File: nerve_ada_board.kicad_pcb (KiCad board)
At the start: 4 copper layers, 100 x 100 mm, 66 parts, among them J1 TC2050-IDC, J10 PC1-3, J11 PB4-5, J12 Camera, J2 472192001, J3 2171750001, J6 WS2812B, J7 CAN1, J8 CAN2, J9 PA4-7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

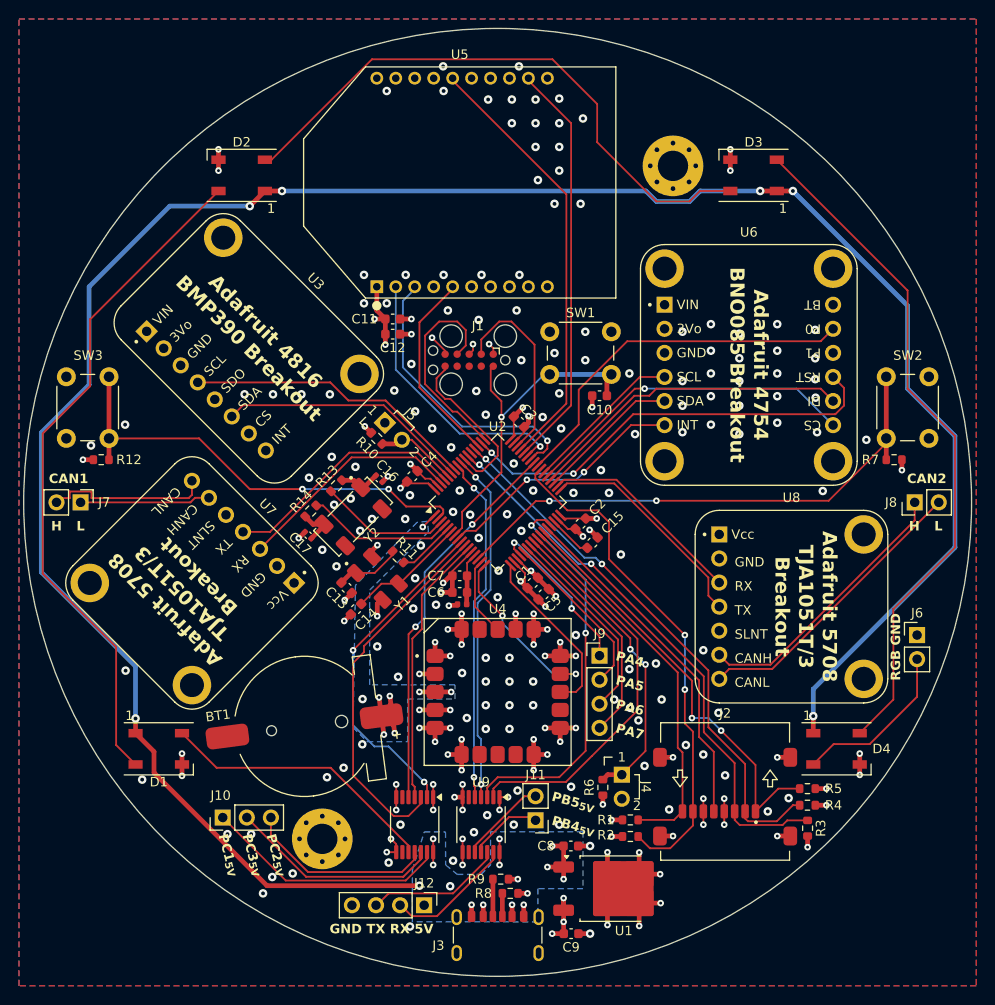
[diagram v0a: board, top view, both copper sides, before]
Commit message: Add GND plane stitching and cleanup layout
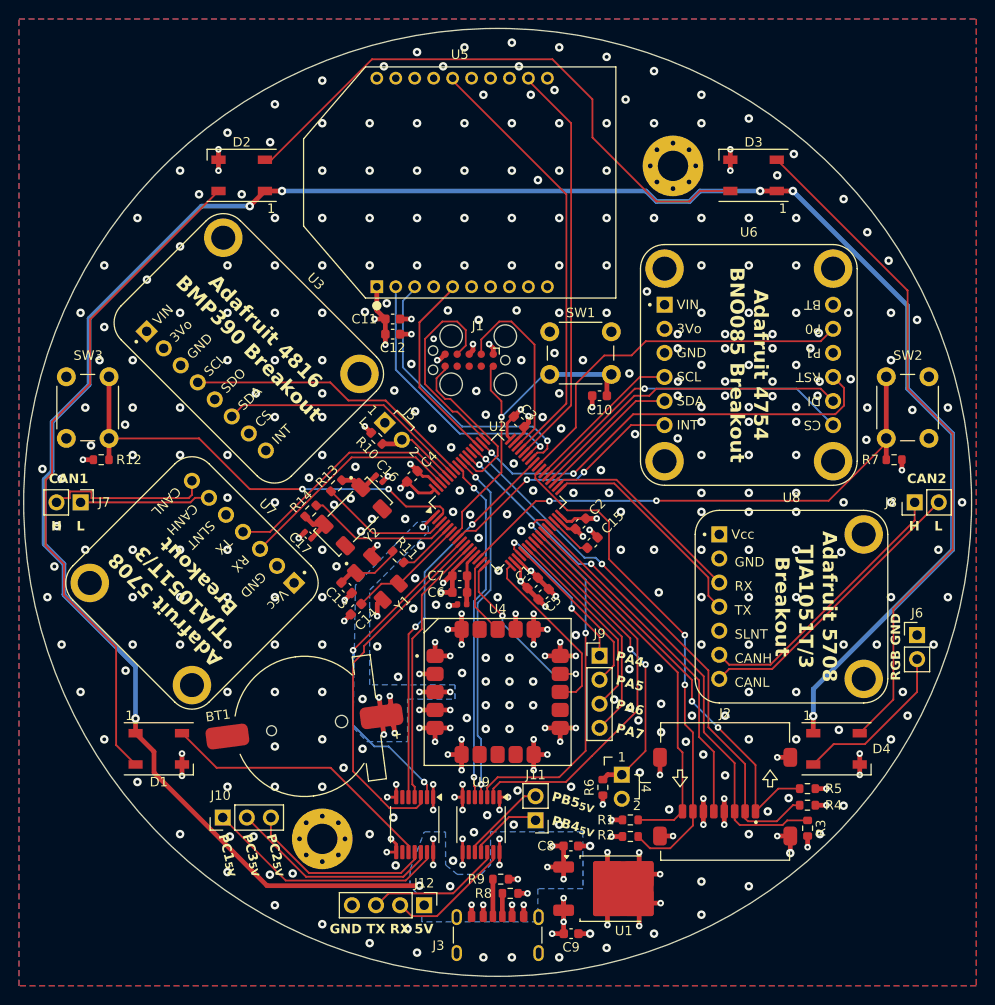
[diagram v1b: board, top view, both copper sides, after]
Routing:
- net +5V: track 255.4 -> 253.0 mm
- net /SDIO_D2: track 45.4 -> 44.4 mm
- net /PC2: track 39.3 -> 38.4 mm
- net /GPIO_IMU_P0: track 39.4 -> 39.9 mm
- net GND: track 126.7 -> 126.3 mm, vias 233 -> 402

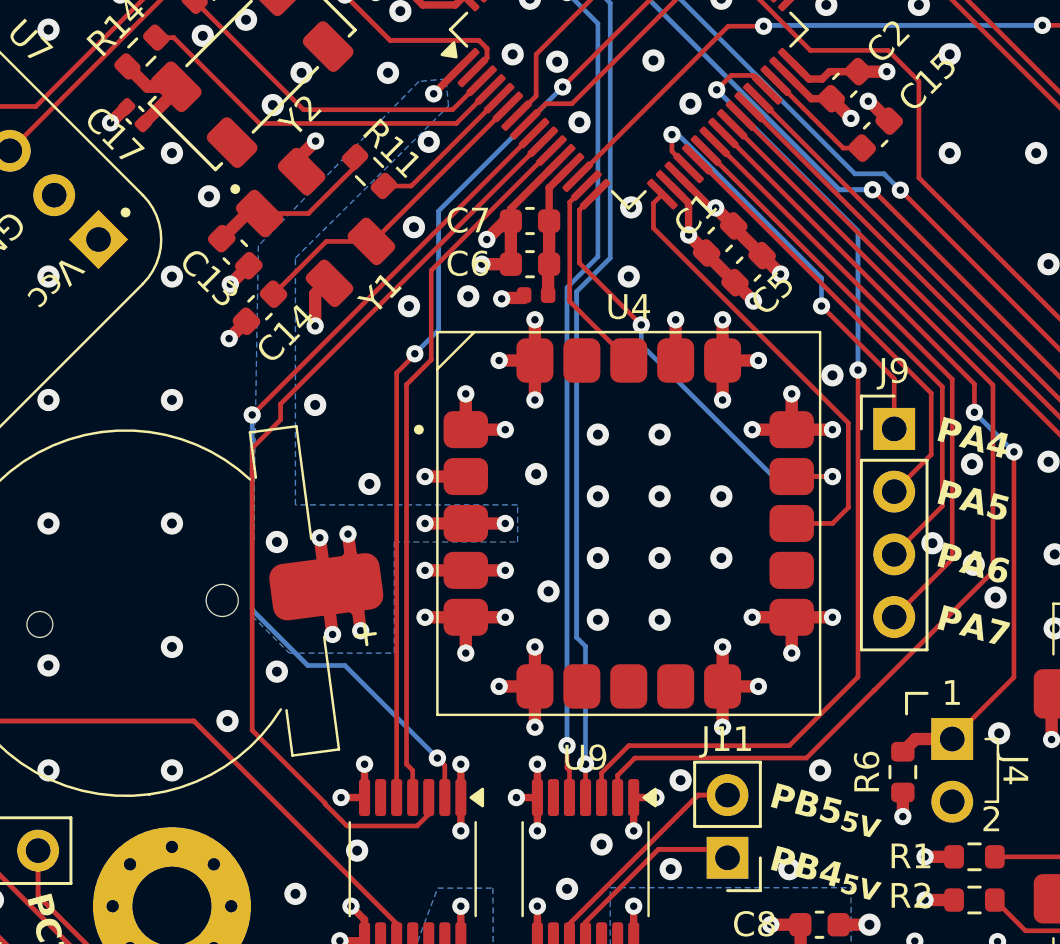
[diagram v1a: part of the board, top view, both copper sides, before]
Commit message: Final cleanup, fix stackup, adjust page docs
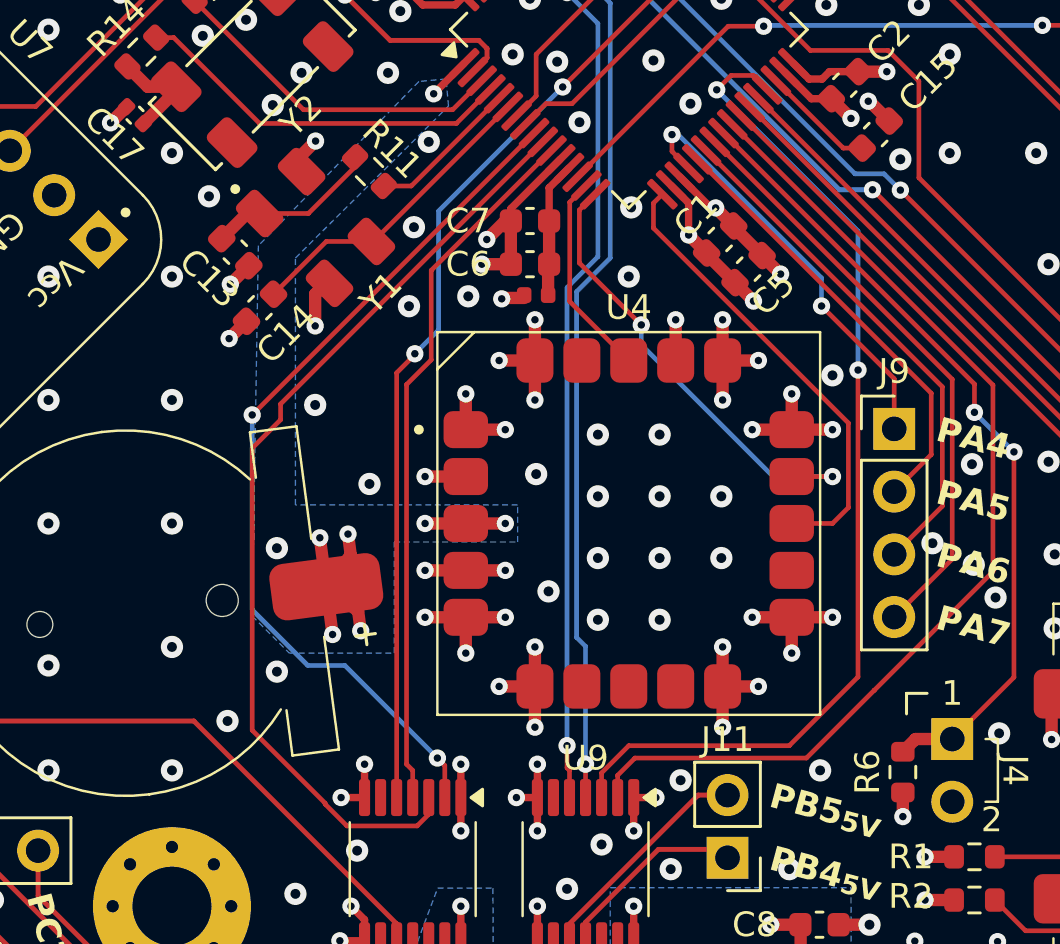
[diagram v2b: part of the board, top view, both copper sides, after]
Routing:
- net GND: vias 402 -> 403
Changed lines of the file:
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@@
 	(generator_version "8.0")
 	(general
-		(thickness 1.58)
+		(thickness 1.59648)
 		(legacy_teardrops no)
 	)
 	(paper "A4")
+	(title_block
+		(title "Nerve ADA Board")
+		(rev "0.1.0-alpha")
+		(company "Daniel Jeon")
+		(comment 1 "Stackup: JLC041611-7628 (1oz outer, 1oz inner)")
+	)
 	(layers
 		(0 "F.Cu" signal)
@@
 			(layer "F.Mask"
 				(type "Top Solder Mask")
-				(thickness 0.01)
+				(thickness 0.01524)
 			)
 			(layer "F.Cu"
@@
 				(type "prepreg")
 				(color "FR4 natural")
-				(thickness 0.11)
-				(material "2116")
-				(epsilon_r 4.29)
+				(thickness 0.203)
+				(material "7628")
+				(epsilon_r 4.4)
 				(loss_tangent 0.02)
 			)
 			(layer "In1.Cu"
 				(type "copper")
-				(thickness 0.035)
+				(thickness 0.03)
 			)
 			(layer "dielectric 2"
 				(type "core")
-				(thickness 1.2)
+				(thickness 1.03)
 				(material "FR4")
 				(epsilon_r 4.6)
@@
 			(layer "In2.Cu"
 				(type "copper")
-				(thickness 0.035)
+				(thickness 0.03)
 			)
 			(layer "dielectric 3"
 				(type "prepreg")
 				(color "FR4 natural")
-				(thickness 0.11)
-				(material "2116")
-				(epsilon_r 4.29)
+				(thickness 0.203)
+				(material "7628")
+				(epsilon_r 4.4)
 				(loss_tangent 0.02)
 			)
@@
 			(layer "B.Mask"
 				(type "Bottom Solder Mask")
-				(thickness 0.01)
+				(thickness 0.01524)
 			)
 			(layer "B.Paste"
@@
 		(fp_arc
 			(start -4.68596 5.727284)
-			(mid -6.687151 3.168902)
+			(mid -6.687149 3.1689)
 			(end -7.4 0)
 			(stroke
@@
 	)
 	(via
-		(at 134.25 125.75)
+		(at 134.25 126)
 		(size 0.9)
 		(drill 0.4)
@@
 	)
 	(via
+		(at 159.5 110.25)
+		(size 0.9)
+		(drill 0.4)
+		(layers "F.Cu" "B.Cu")
+		(free yes)
+		(net 1)
+	)
+	(via
 		(at 142.125238 90.000001)
 		(size 0.7)
@@
 	)
 	(segment
-		(start 104.5 105)
-		(end 116.087943 105)
+		(start 116.568199 104.519744)
+		(end 118.046051 104.519744)
 		(width 0.2)
 		(layer "F.Cu")
@@
 	)
 	(segment
-		(start 116.568199 104.519744)
-		(end 118.046051 104.519744)
+		(start 104.5 105)
+		(end 116.087943 105)
 		(width 0.2)
 		(layer "F.Cu")
@@
 	)
 	(segment
-		(start 103.35 104.55)
-		(end 103.35 103.85)
+		(start 115.901545 104.55)
+		(end 116.25 104.201545)
 		(width 0.2)
 		(layer "F.Cu")
@@
 	)
 	(segment
-		(start 103.35 103.85)
-		(end 105.65 103.85)
+		(start 101.96 105)
+		(end 102.41 104.55)
 		(width 0.2)
 		(layer "F.Cu")
@@
 	)
 	(segment
-		(start 102.41 104.55)
-		(end 103.35 104.55)
+		(start 103.35 103.85)
+		(end 105.65 103.85)
 		(width 0.2)
 		(layer "F.Cu")
@@
 	)
 	(segment
-		(start 115.901545 104.55)
-		(end 116.25 104.201545)
+		(start 105.65 104.55)
+		(end 115.901545 104.55)
 		(width 0.2)
 		(layer "F.Cu")
@@
 	)
 	(segment
-		(start 105.65 103.85)
-		(end 105.65 104.55)
+		(start 102.41 104.55)
+		(end 103.35 104.55)
 		(width 0.2)
 		(layer "F.Cu")
@@
 	)
 	(segment
-		(start 101.96 105)
-		(end 102.41 104.55)
+		(start 103.35 104.55)
+		(end 103.35 103.85)
 		(width 0.2)
 		(layer "F.Cu")
@@
 	)
 	(segment
-		(start 105.65 104.55)
-		(end 115.901545 104.55)
+		(start 105.65 103.85)
+		(end 105.65 104.55)
 		(width 0.2)
 		(layer "F.Cu")
@@
 	)
 	(segment
-		(start 177.278604 122.124999)
-		(end 192.5 106.903603)
+		(start 172.924999 122.124999)
+		(end 177.278604 122.124999)
 		(width 0.2)
 		(layer "F.Cu")
@@
 	)
 	(segment
-		(start 171.88 121.08)
-		(end 172.924999 122.124999)
+		(start 177.278604 122.124999)
+		(end 192.5 106.903603)
 		(width 0.2)
 		(layer "F.Cu")
@@
 	)
 	(segment
-		(start 172.924999 122.124999)
-		(end 177.278604 122.124999)
+		(start 171.88 121.08)
+		(end 172.924999 122.124999)
 		(width 0.2)
 		(layer "F.Cu")

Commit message: Clean up silkscreen, fill mounting hole reliefs
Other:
- board text added: "M3"
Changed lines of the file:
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@@
 		(tags "inductor")
 		(property "Reference" "L1"
-			(at 1.8 0.01 0)
+			(at -2.5 0 0)
 			(layer "F.SilkS")
-			(hide yes)
 			(effects
 				(font
@@
 		(tags "capacitor")
 		(property "Reference" "C15"
-			(at 3 0 -135)
+			(at 3 0 225)
 			(layer "F.SilkS")
 			(effects
@@
 		(tags "capacitor")
 		(property "Reference" "C16"
-			(at 0 -1.2 135)
+			(at 2.5 0 135)
 			(layer "F.SilkS")
 			(effects
@@
 		(tags "LQFP QFP")
 		(property "Reference" "U2"
-			(at 5.656854 -5.656854 0)
+			(at 5.75 -5.75 0)
 			(layer "F.SilkS")
 			(effects
@@
 		(tags "resistor")
 		(property "Reference" "R11"
-			(at 0 1.3 135)
+			(at 0 1.5 135)
 			(layer "F.SilkS")
 			(effects
@@
 		(tags "capacitor")
 		(property "Reference" "C3"
-			(at 0 -1.43 135)
+			(at 0 -1.5 135)
 			(layer "F.SilkS")
 			(effects
@@
 		(tags "capacitor")
 		(property "Reference" "C17"
-			(at 0 -1.2 135)
+			(at -2.5 0 135)
 			(layer "F.SilkS")
 			(effects
@@
 		(tags "capacitor")
 		(property "Reference" "C5"
-			(at 0 -1.399999 45)
+			(at -2.5 0 45)
 			(layer "F.SilkS")
 			(effects
@@
 		(sheetname "Root")
 		(sheetfile "nerve_ada_board.kicad_sch")
+		(zone_connect 2)
 		(attr exclude_from_pos_files exclude_from_bom)
 		(fp_circle
@@
 		(fp_arc
 			(start -4.68596 5.727284)
-			(mid -6.687149 3.1689)
+			(mid -6.687148 3.1689)
 			(end -7.4 0)
 			(stroke
@@
 		(tags "LED RGB NeoPixel PLCC-4 5050")
 		(property "Reference" "D1"
-			(at 0.000001 3.5 0)
+			(at 0.000001 -3.5 0)
 			(layer "F.SilkS")
 			(effects
@@
 		(at 135.815685 113.012742 -45)
 		(property "Reference" "Y1"
-			(at 3.749999 0 -135)
+			(at 3.749999 0 225)
 			(layer "F.SilkS")
 			(effects
@@
 		(sheetname "Root")
 		(sheetfile "nerve_ada_board.kicad_sch")
+		(zone_connect 2)
 		(attr exclude_from_pos_files exclude_from_bom)
 		(fp_circle
@@
 		(tags "LED RGB NeoPixel PLCC-4 5050")
 		(property "Reference" "D4"
-			(at 4.75 0 0)
+			(at 0.000001 -3.5 0)
 			(layer "F.SilkS")
 			(effects
@@
 		(tags "capacitor")
 		(property "Reference" "C1"
-			(at 0 1.399999 45)
+			(at -2.5 0 45)
 			(layer "F.SilkS")
 			(effects
@@
 		(at 144.5 71.25 90)
 		(property "Reference" "U5"
-			(at 13.5 0 0)
+			(at 13.25 0 0)
 			(unlocked yes)
 			(layer "F.SilkS")
@@
 			(unlocked yes)
 			(layer "F.SilkS")
-			(hide yes)
 			(effects
 				(font
@@
 		)
 		(property "Manufacturer" "Texas Instruments"
-			(at 0 0 90)
+			(at 0 0 -90)
 			(layer "F.Fab")
 			(hide yes)
@@
 		)
 		(property "Manufacturer Part Number" "TXB0104QPWRQ1"
-			(at 0 0 90)
+			(at 0 0 -90)
 			(layer "F.Fab")
 			(hide yes)
@@
 		(tags "capacitor")
 		(property "Reference" "C12"
-			(at 0 1.43 0)
+			(at 0 1.5 0)
 			(layer "F.SilkS")
 			(effects
@@
 		)
 	)
+	(gr_text "M3"
+		(at 167 73.7 0)
+		(layer "F.SilkS")
+		(effects
+			(font
+				(size 1 1)
+				(thickness 0.125)
+			)
+		)
+	)
 	(gr_text "GND TX RX 5V"
 		(at 136.25 150 0)
@@
 			)
 		)
+	)
+	(gr_text "M3"
+		(at 130 144.7 0)
+		(layer "F.SilkS")
+		(effects
+			(font
+				(size 1 1)
+				(thickness 0.125)
+			)
+		)
